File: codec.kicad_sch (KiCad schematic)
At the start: 19 parts, among them IC1 TLV320AIC3204IRHBR

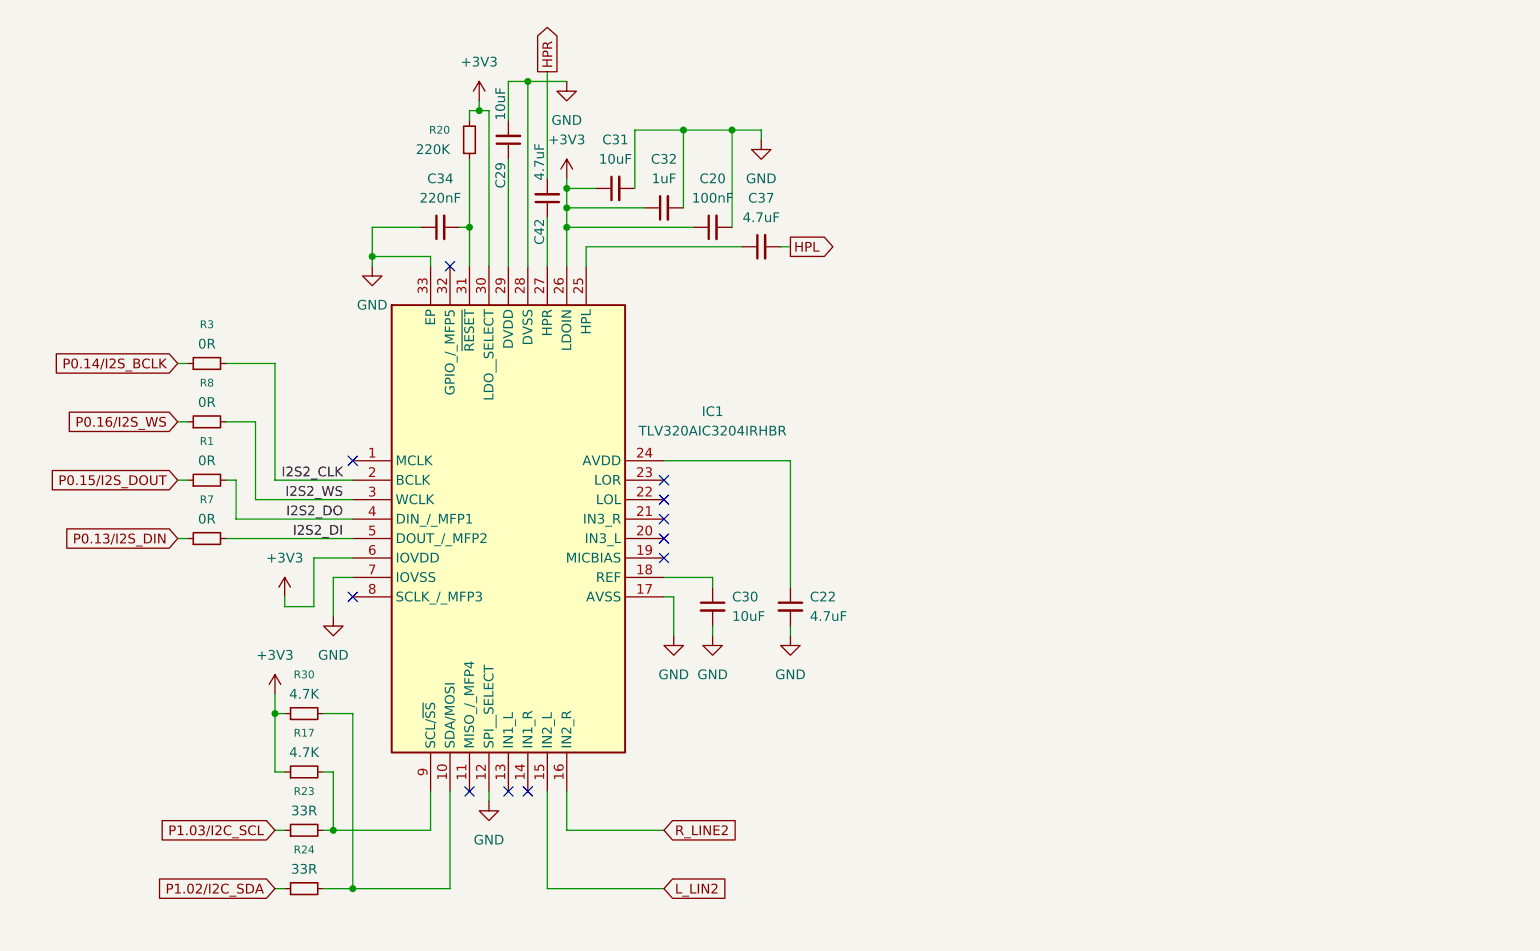
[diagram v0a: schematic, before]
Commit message: schematic completed
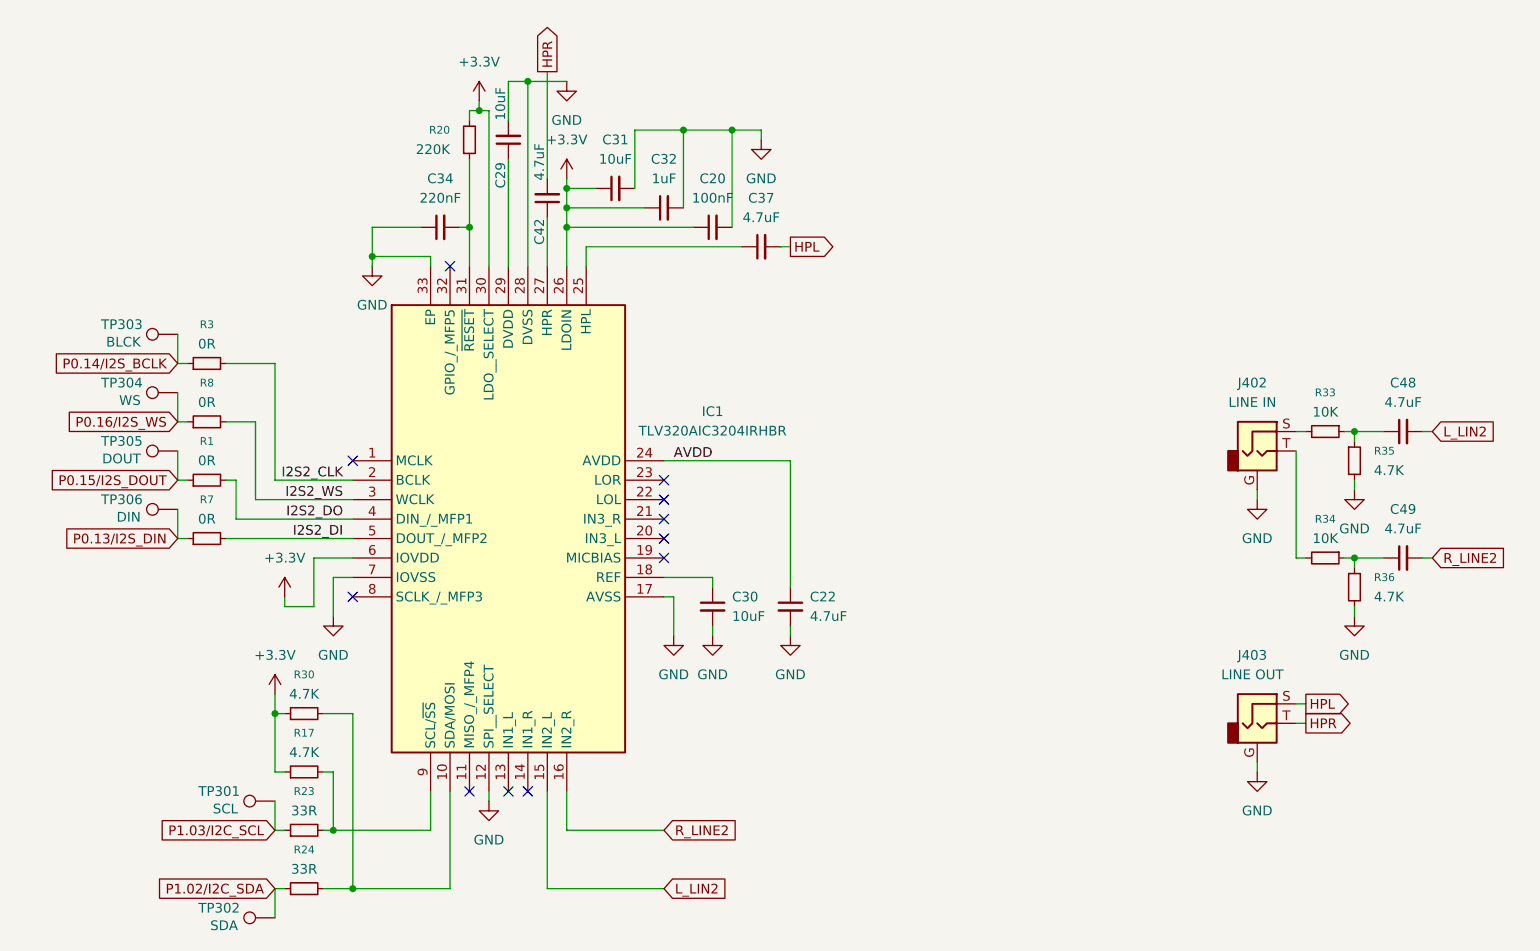
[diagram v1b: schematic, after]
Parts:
- added C48, C49: 4.7uF, Capacitor_SMD:C_0603_1608Metric_Pad1.08x0.95mm_HandSolder, symbol Device:C_Small
- added J402: LINE IN, XKB_PJ-3200:XKB_PJ-3200, symbol Connector_Audio:AudioJack2_Ground
- added J403: LINE OUT, XKB_PJ-3200:XKB_PJ-3200, symbol Connector_Audio:AudioJack2_Ground
- added R33, R34: 10K, Resistor_SMD:R_0603_1608Metric_Pad0.98x0.95mm_HandSolder, symbol Device:R_Small
- added R35, R36: 4.7K, Resistor_SMD:R_0603_1608Metric_Pad0.98x0.95mm_HandSolder, symbol Device:R_Small
- added TP301: SCL, TestPoint:TestPoint_THTPad_1.0x1.0mm_Drill0.5mm, symbol Connector:TestPoint
- added TP302: SDA, TestPoint:TestPoint_THTPad_1.0x1.0mm_Drill0.5mm, symbol Connector:TestPoint
- added TP303: BLCK, TestPoint:TestPoint_THTPad_1.0x1.0mm_Drill0.5mm, symbol Connector:TestPoint
- added TP304: WS, TestPoint:TestPoint_THTPad_1.0x1.0mm_Drill0.5mm, symbol Connector:TestPoint
- added TP305: DOUT, TestPoint:TestPoint_THTPad_1.0x1.0mm_Drill0.5mm, symbol Connector:TestPoint
- added TP306: DIN, TestPoint:TestPoint_THTPad_1.0x1.0mm_Drill0.5mm, symbol Connector:TestPoint
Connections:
- net GND: now also J402.G, J403.G, R35.2, R36.2
- net HPL: now also J403.S
- net HPR: now also J403.T
- net L_LIN2: now also C48.2
- net P0.13/I2S_DIN: now also TP306.1
- net P0.14/I2S_BCLK: now also TP303.1
- net P0.15/I2S_DOUT: now also TP305.1
- net P0.16/I2S_WS: now also TP304.1
- net P1.02/I2C_SDA: now also TP302.1
- net P1.03/I2C_SCL: now also TP301.1
- net R_LINE2: now also C49.2
- net AVDD: now reaches C22.1, IC1.24 (AVDD)
- net +3V3 renamed +3.3V
- new net: J402.S, R33.2
- new net: J402.T, R34.2
- new net: C49.1, R34.1, R36.1
- new net: C48.1, R33.1, R35.1

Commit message: FINALISED LAYOUT
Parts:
- added TP304: LOR, TestPoint:TestPoint_THTPad_1.0x1.0mm_Drill0.5mm, symbol Connector:TestPoint
- added TP306: LOL, TestPoint:TestPoint_THTPad_1.0x1.0mm_Drill0.5mm, symbol Connector:TestPoint
- renumbered C29 to C301, C31 to C302, C42 to C303, C32 to C304, C34 to C305, C20 to C306, C37 to C307, C48 to C308, C49 to C309, C30 to C310, C22 to C311, IC1 to IC301, J402 to J301, J403 to J302, R20 to R301, R3 to R302, R8 to R303, R33 to R304, R35 to R305, R1 to R306, R7 to R307, R34 to R308, R36 to R309, R30 to R310, R17 to R311, R23 to R312, R24 to R313, TP303 to TP301, TP304 to TP302, TP305 to TP303, TP306 to TP305, TP301 to TP307, TP302 to TP308
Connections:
- net at IC301.22 (LOL): now also TP306.1
- net at IC301.23 (LOR): now also TP304.1
- net L_LIN2 renamed L_LINE2
- no-connect marks 11 -> 9

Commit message: finalised layout
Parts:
- renumbered C302 to C10, C303 to C11, C304 to C12, C305 to C13, C306 to C14, C307 to C15, C308 to C16, C309 to C17, C310 to C18, C311 to C19, C301 to C9, IC301 to IC1, J301 to J3, J302 to J4, R301 to R11, R302 to R12, R303 to R13, R304 to R14, R305 to R15, R306 to R16, R307 to R17, R308 to R18, R309 to R19, R310 to R20, R311 to R21, R312 to R22, R313 to R23, TP304 to TP10, TP305 to TP11, TP306 to TP12, TP307 to TP13, TP308 to TP14, TP301 to TP7, TP302 to TP8, TP303 to TP9
